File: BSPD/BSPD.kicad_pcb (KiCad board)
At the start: 2 copper layers, 54 x 46 mm, 82 parts, among them J1 Conn_01x15_Pin, J2 Conn_01x15_Pin, U1 TLV2371DBV, U10 TLV2371DBV, U13 74LVC1G08, U14 AP2204K-ADJ, U15 AP7375Q-50WR-7, U17 74LVC1G08, U18 74LVC1G08, U2 TLV2371DBV, U3 TLV2371DBV, U4 TLV2371DBV, U8 TLV2371DBV, U9 TLV2371DBV

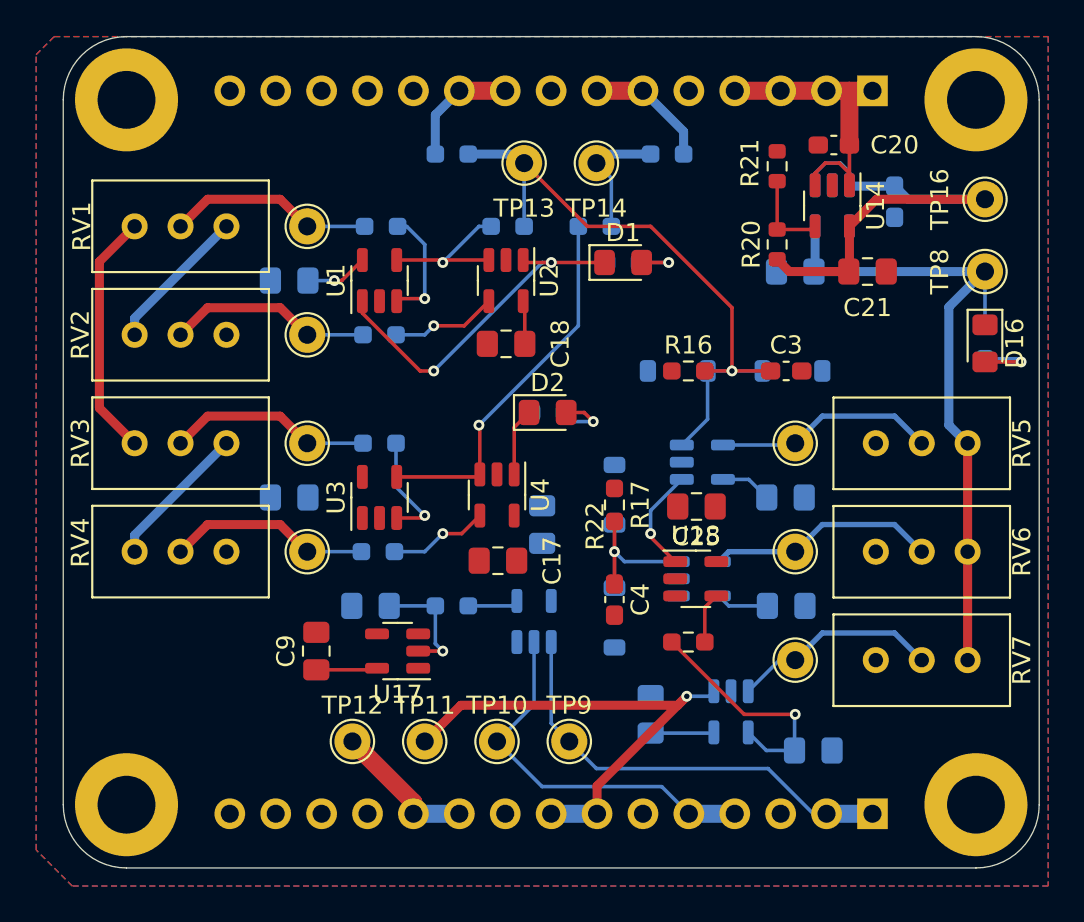
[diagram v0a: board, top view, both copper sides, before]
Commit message: BSPD v3 finish basic layout
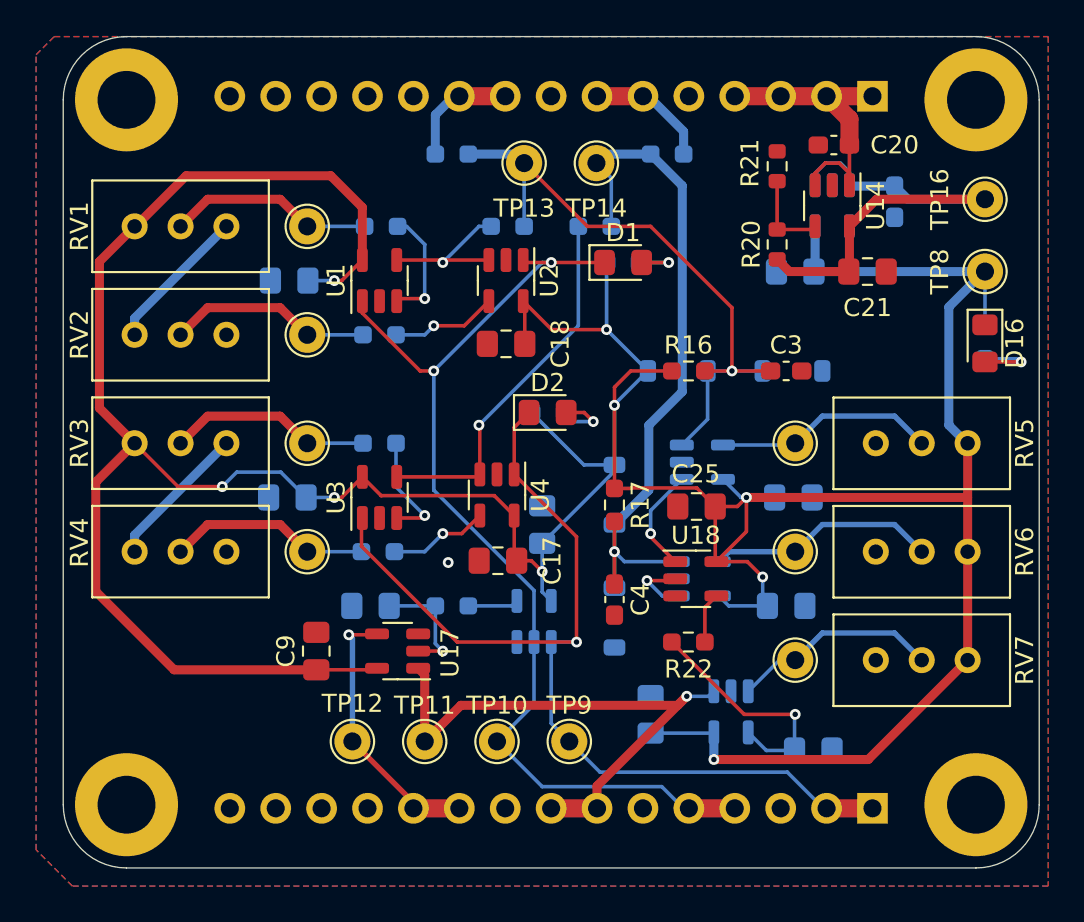
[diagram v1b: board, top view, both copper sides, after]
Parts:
- moved C15 0.44 mm to (99.6, 141.2)
- moved J1 0.30 mm to (104.0, 119.0)
- moved J2 0.30 mm to (104.0, 158.4)
- moved C16 0.10 mm to (71.6, 141.2)
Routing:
- net +5V: track 69.9 -> 231.7 mm, vias 1 -> 9
- net Brake_Limit_Check_out: track 28.1 -> 56.1 mm, vias 0 -> 1
- net brake: track 17.7 -> 40.5 mm
- net Current_Limit_Check_out: track 40.2 -> 57.5 mm
- net BSPD: track 7.94 -> 15.2 mm, vias 0 -> 1
- net Simultaneous_brake&current: track 28.2 -> 32.4 mm
- net Net-(U18-Pad2): track 0.00 -> 3.66 mm, vias 0 -> 1
- net GND: vias 0 -> 1

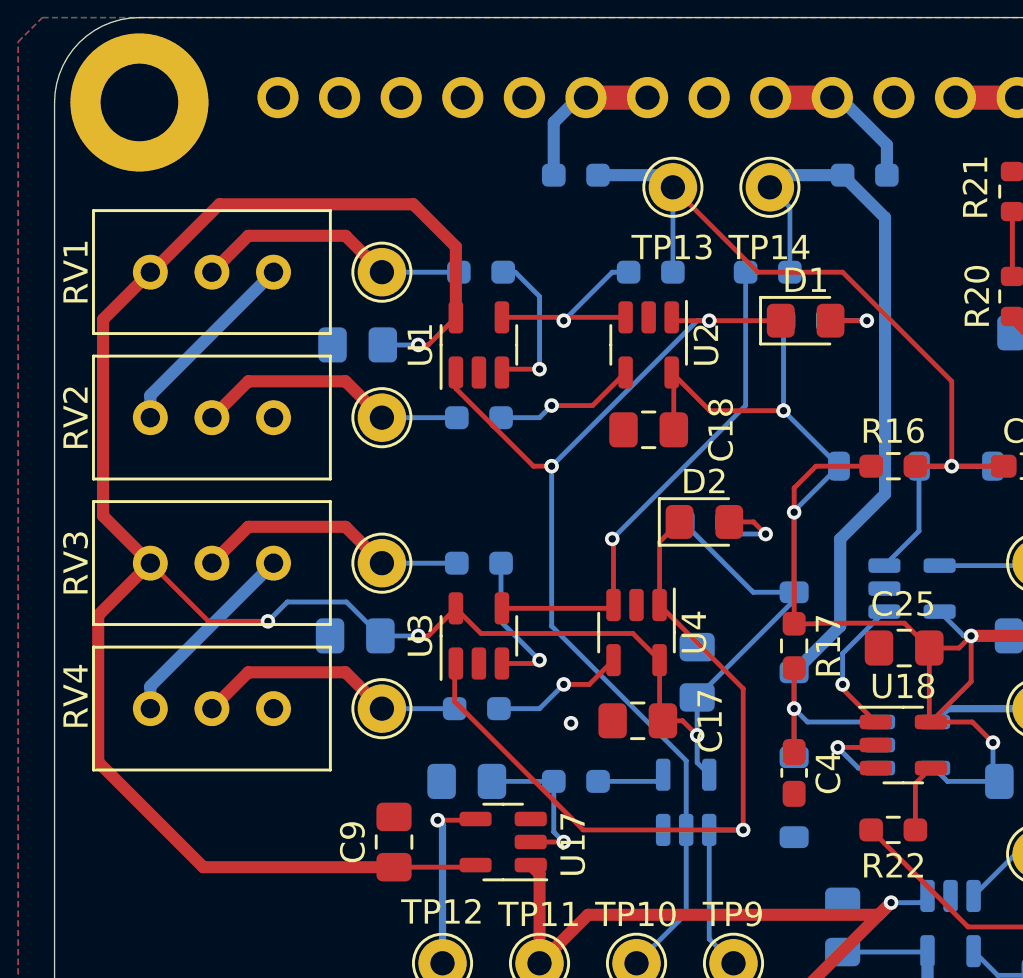
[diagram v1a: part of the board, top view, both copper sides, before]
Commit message: Add And gate and R at limit chack
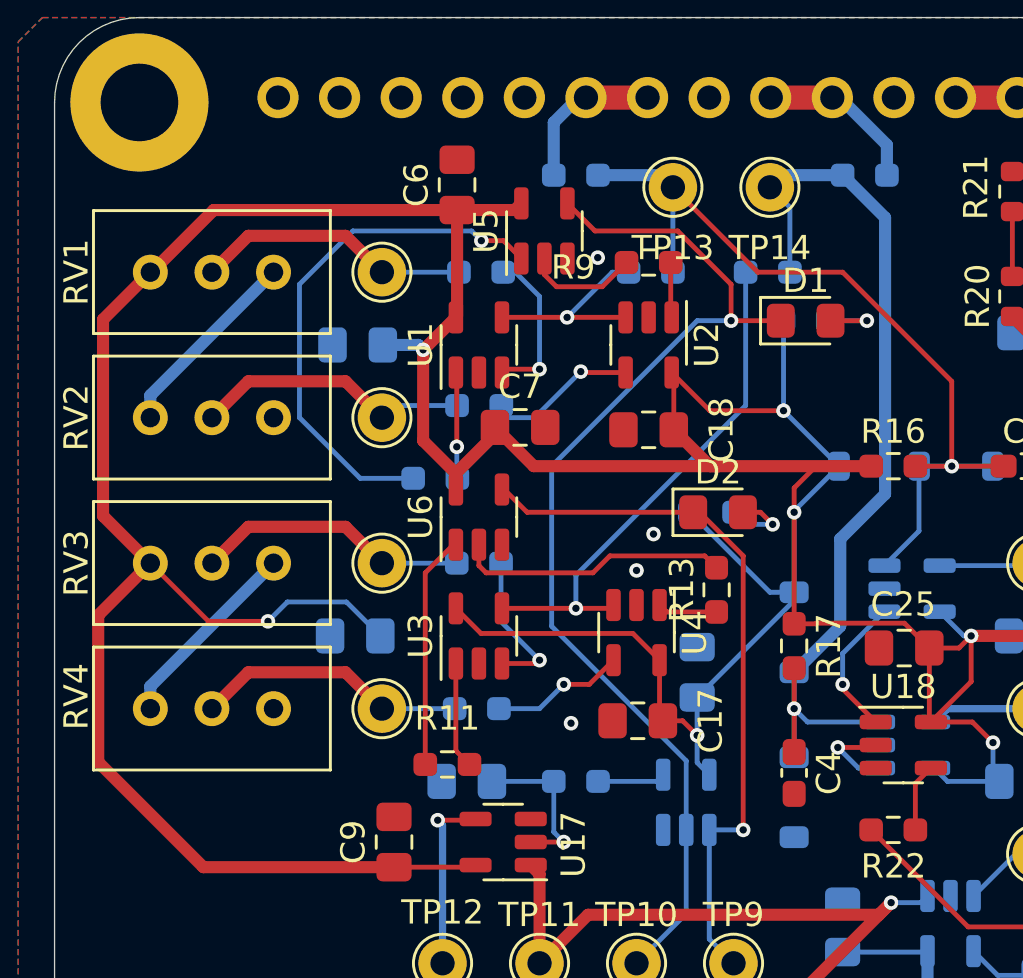
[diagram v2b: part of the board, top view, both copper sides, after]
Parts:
- added C6: 10u, Capacitor_SMD:C_0805_2012Metric_Pad1.18x1.45mm_HandSolder, F.Cu at (75.8, 122.6)
- added C7: 10u, Capacitor_SMD:C_0805_2012Metric_Pad1.18x1.45mm_HandSolder, F.Cu at (78.4, 132.6)
- added R11: 10k, Resistor_SMD:R_0603_1608Metric_Pad0.98x0.95mm_HandSolder, F.Cu at (75.4, 146.5)
- added R13: 10k, Resistor_SMD:R_0603_1608Metric_Pad0.98x0.95mm_HandSolder, F.Cu at (86.5, 139.3)
- added R7: 10k, Resistor_SMD:R_0603_1608Metric_Pad0.98x0.95mm_HandSolder, B.Cu at (74.9, 134.7)
- added R9: 10k, Resistor_SMD:R_0603_1608Metric_Pad0.98x0.95mm_HandSolder, F.Cu at (83.7, 125.8)
- added U5: 74LVC1G08, Package_TO_SOT_SMD:SOT-23-5, F.Cu at (79.4, 124.5)
- added U6: 74LVC1G08, Package_TO_SOT_SMD:SOT-23-5, F.Cu at (76.7, 136.3)
- moved D2 0.69 mm to (86.6, 136.1)
- moved R3 0.50 mm to (76.7, 131.7)
- moved R10 0.49 mm to (86.3, 136.1)
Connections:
- U1 pad 1: Current_Limit_Check_out -> Net-(R7-Pad1)
- U2 pad 1: Current_Limit_Check_out -> Net-(R9-Pad1)
- U3 pad 1: Brake_Limit_Check_out -> Net-(R11-Pad1)
- U4 pad 1: Brake_Limit_Check_out -> Net-(R13-Pad1)
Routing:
- net +5V: track 231.7 -> 259.2 mm, vias 9 -> 8
- net Net-(R7-Pad2): track 0.00 -> 21.8 mm, vias 0 -> 1
- net Net-(R13-Pad2): track 0.00 -> 11.1 mm
- net Net-(R11-Pad2): track 0.00 -> 9.69 mm
- net Brake_Limit_Check_out: track 56.1 -> 48.3 mm
- net Net-(R9-Pad2): track 0.00 -> 4.67 mm
- net Net-(R11-Pad1): track 0.00 -> 4.47 mm
- net Net-(R7-Pad1): track 0.00 -> 4.31 mm, vias 0 -> 1
- net Net-(R13-Pad1): track 0.00 -> 2.52 mm
- net Net-(R9-Pad1): track 0.00 -> 2.47 mm
- net Current_Limit_Check_out: track 57.5 -> 59.6 mm, vias 2 -> 1
- net Net-(U3--): track 20.7 -> 21.4 mm
- net GND: vias 1 -> 4

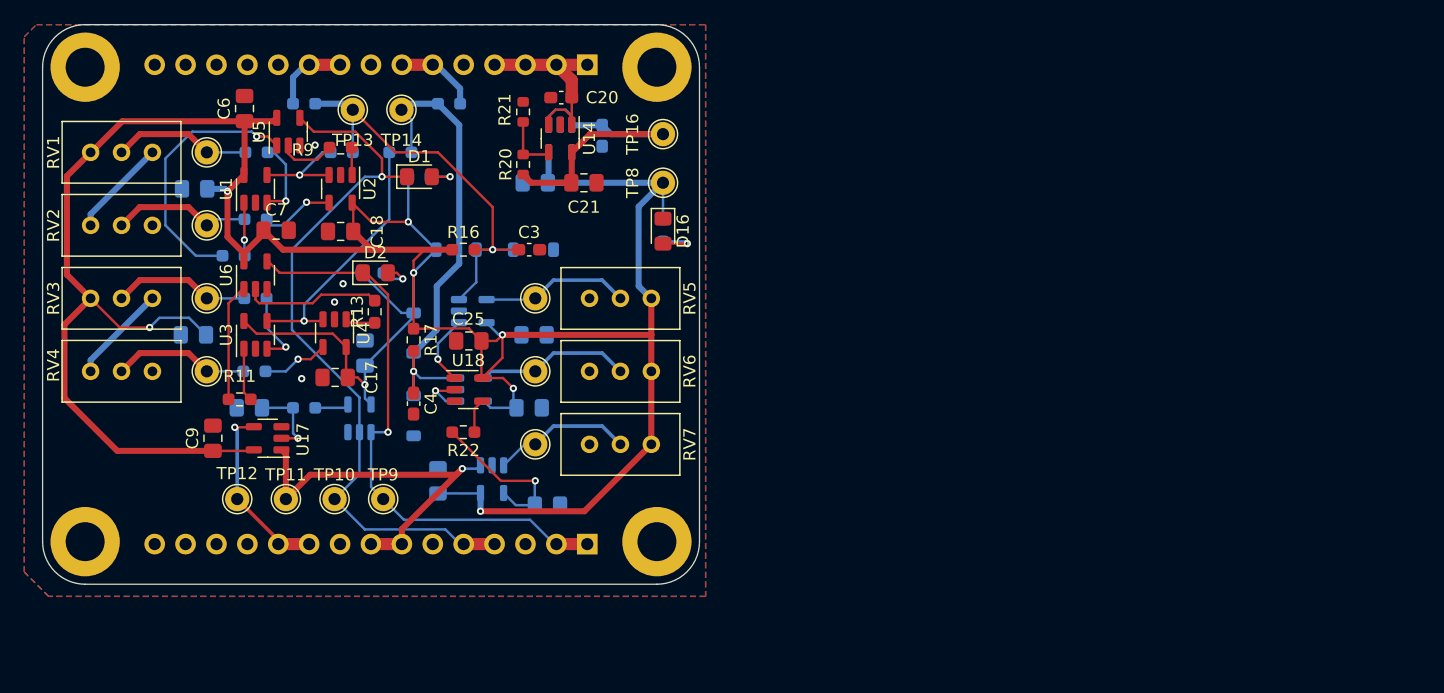
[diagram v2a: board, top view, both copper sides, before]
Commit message: BSPD v.3.2 change pin header to 02*10
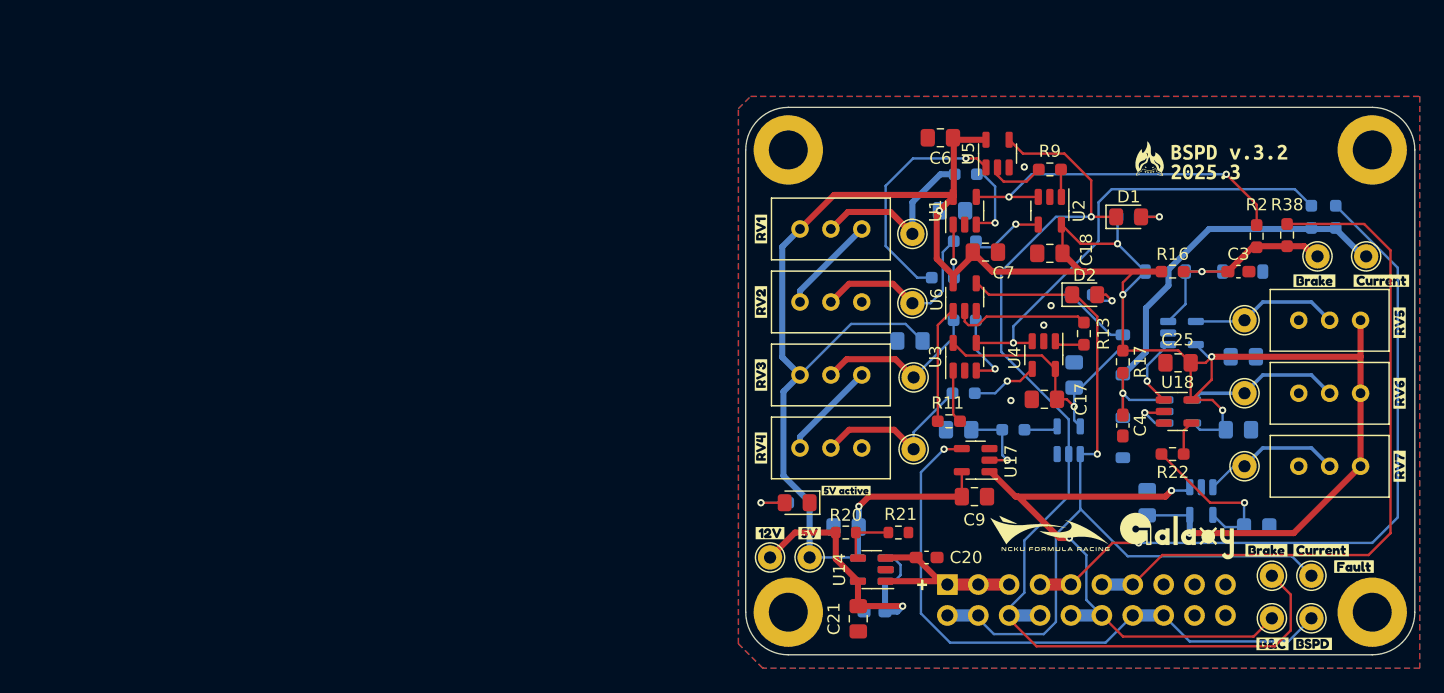
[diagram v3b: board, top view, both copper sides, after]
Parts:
- removed J1: Conn_01x15_Pin, Connector_PinHeader_2.54mm:PinHeader_1x15_P2.54mm_Vertical
- added G***: LOGO, logo:fire_shark_4mm, F.Cu at (150.2, 126.8)
- added G***: LOGO, logo:nckufs_logo_10mm, F.Cu at (142.0, 157.5)
- added G***: LOGO, logo:galaxy_logo_10mm, F.Cu at (152.5, 157.8)
- added kibuzzard-67D12800: G***, kibuzzard-67D12800, F.Cu at (163.6, 166.6)
- added kibuzzard-67D1282F: G***, kibuzzard-67D1282F, F.Cu at (160.3, 166.6)
- added kibuzzard-67D1286B: G***, kibuzzard-67D1286B, F.Cu at (159.8, 158.9)
- added kibuzzard-67D12885: G***, kibuzzard-67D12885, F.Cu at (164.3, 158.9)
- added kibuzzard-67D1289B: G***, kibuzzard-67D1289B, F.Cu at (170.7, 140.2)
- added kibuzzard-67D128B9: G***, kibuzzard-67D128B9, F.Cu at (170.7, 146.0)
- added kibuzzard-67D128E6: G***, kibuzzard-67D128E6, F.Cu at (170.8, 152.0)
- added kibuzzard-67D12931: G***, kibuzzard-67D12931, F.Cu at (118.2, 132.5)
- added kibuzzard-67D1293D: G***, kibuzzard-67D1293D, F.Cu at (118.2, 138.5)
- added kibuzzard-67D12947: G***, kibuzzard-67D12947, F.Cu at (118.3, 144.5)
- added kibuzzard-67D12954: G***, kibuzzard-67D12954, F.Cu at (118.2, 150.5)
- added kibuzzard-67D12976: G***, kibuzzard-67D12976, F.Cu at (163.8, 136.8)
- added kibuzzard-67D1299E: G***, kibuzzard-67D1299E, F.Cu at (169.2, 136.8)
- added kibuzzard-67D129F2: G***, kibuzzard-67D129F2, F.Cu at (167.0, 160.2)
- added kibuzzard-67D12A07: G***, kibuzzard-67D12A07, F.Cu at (119.0, 157.5)
- added kibuzzard-67D12A20: G***, kibuzzard-67D12A20, F.Cu at (122.2, 157.5)
- added kibuzzard-67D12A37: G***, kibuzzard-67D12A37, F.Cu at (125.2, 154.0)
- added kibuzzard-67D12B34: G***, kibuzzard-67D12B34, F.Cu at (131.5, 161.8)
- added kibuzzard-67D12B65: G***, kibuzzard-67D12B65, F.Cu at (156.8, 127.0)
- J2: value Conn_01x15_Pin -> Conn_02x10_Odd_Even; footprint Connector_PinHeader_2.54mm:PinHeader_1x15_P2.54mm_Vertical -> Connector_PinHeader_2.54mm:PinHeader_2x10_P2.54mm_Vertical
- R2, R38: moved to F.Cu
- moved TP12 88.8 mm to (163.5, 164.5)
- moved TP11 81.6 mm to (160.2, 164.5)
- moved R38 81.5 mm to (161.5, 133.0), turned to 90 degrees
- moved TP13 80.2 mm to (164.0, 134.8)
- moved TP14 80.2 mm to (168.0, 134.8)
- moved TP10 77.3 mm to (160.2, 161.0)
- moved TP9 76.6 mm to (163.5, 161.0)
- moved R2 75.5 mm to (159.0, 133.1), turned to 90 degrees
- moved R5 75.1 mm to (163.5, 131.5), turned to 90 degrees
- moved R39 73.5 mm to (165.5, 131.5), turned to -90 degrees
- moved C9 62.8 mm to (135.8, 154.5), turned to 0 degrees
- moved C19 62.3 mm to (134.0, 131.0), turned to 0 degrees
- moved H1 59.2 mm to (168.5, 126.0)
- moved H2 59.1 mm to (168.5, 164.0)
- moved C16 58.9 mm to (130.5, 141.7)
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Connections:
- J2 pad 1: Brake_Limit_Check_out -> VDC
- J2 pad 10: BSPD -> Simultaneous_brake&current
- J2 pad 11: BSPD -> Current_init
- J2 pad 12: unconnected-(J2-Pin_12-Pad12) -> Simultaneous_brake&current
- J2 pad 13: GND -> Current_init
- J2 pad 14: GND -> BSPD
- J2 pad 3: unconnected-(J2-Pin_3-Pad3) -> VDC
- J2 pad 4: Current_Limit_Check_out -> Brake_Limit_Check_out
- J2 pad 5: Current_Limit_Check_out -> VDC
- J2 pad 6: unconnected-(J2-Pin_6-Pad6) -> Current_Limit_Check_out
- J2 pad 7: Simultaneous_brake&current -> Brake_init
- J2 pad 8: Simultaneous_brake&current -> Current_Limit_Check_out
- J2 pad 9: unconnected-(J2-Pin_9-Pad9) -> Brake_init
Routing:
- net Brake_init: track 6.97 -> 59.4 mm, vias 0 -> 1
- net Current_init: track 6.89 -> 58.1 mm
- net BSPD: track 15.2 -> 51.6 mm
- net Current_Limit_Check_out: track 59.6 -> 87.6 mm
- net Brake_Limit_Check_out: track 48.3 -> 69.8 mm
- net Net-(U1--): track 8.63 -> 28.9 mm, vias 1 -> 2
- net +5V: track 259.2 -> 240.7 mm
- net current: track 36.5 -> 20.1 mm
- net Net-(U3--): track 21.4 -> 37.6 mm
- net Simultaneous_brake&current: track 32.4 -> 48.5 mm, vias 1 -> 2
- net Net-(R3-Pad1): track 11.6 -> 15.4 mm
- net Net-(R1-Pad1): track 11.4 -> 15.1 mm
- net Net-(R6-Pad1): track 11.3 -> 14.0 mm
- net Net-(R4-Pad1): track 11.3 -> 14.0 mm
- net Net-(R7-Pad2): track 21.8 -> 19.3 mm
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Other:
- board size 54 x 46 mm -> 55 x 45 mm
